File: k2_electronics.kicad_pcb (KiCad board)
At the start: 2 copper layers, 152.1 x 87.5 mm, 58 parts, among them SW1 SW_SPST, SW10 SW_SPST, SW11 SW_SPST, SW12 SW_SPST, SW13 SW_SPST, SW14 SW_SPST, SW15 SW_SPST, SW16 SW_SPST, SW17 SW_SPST, SW18 SW_SPST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

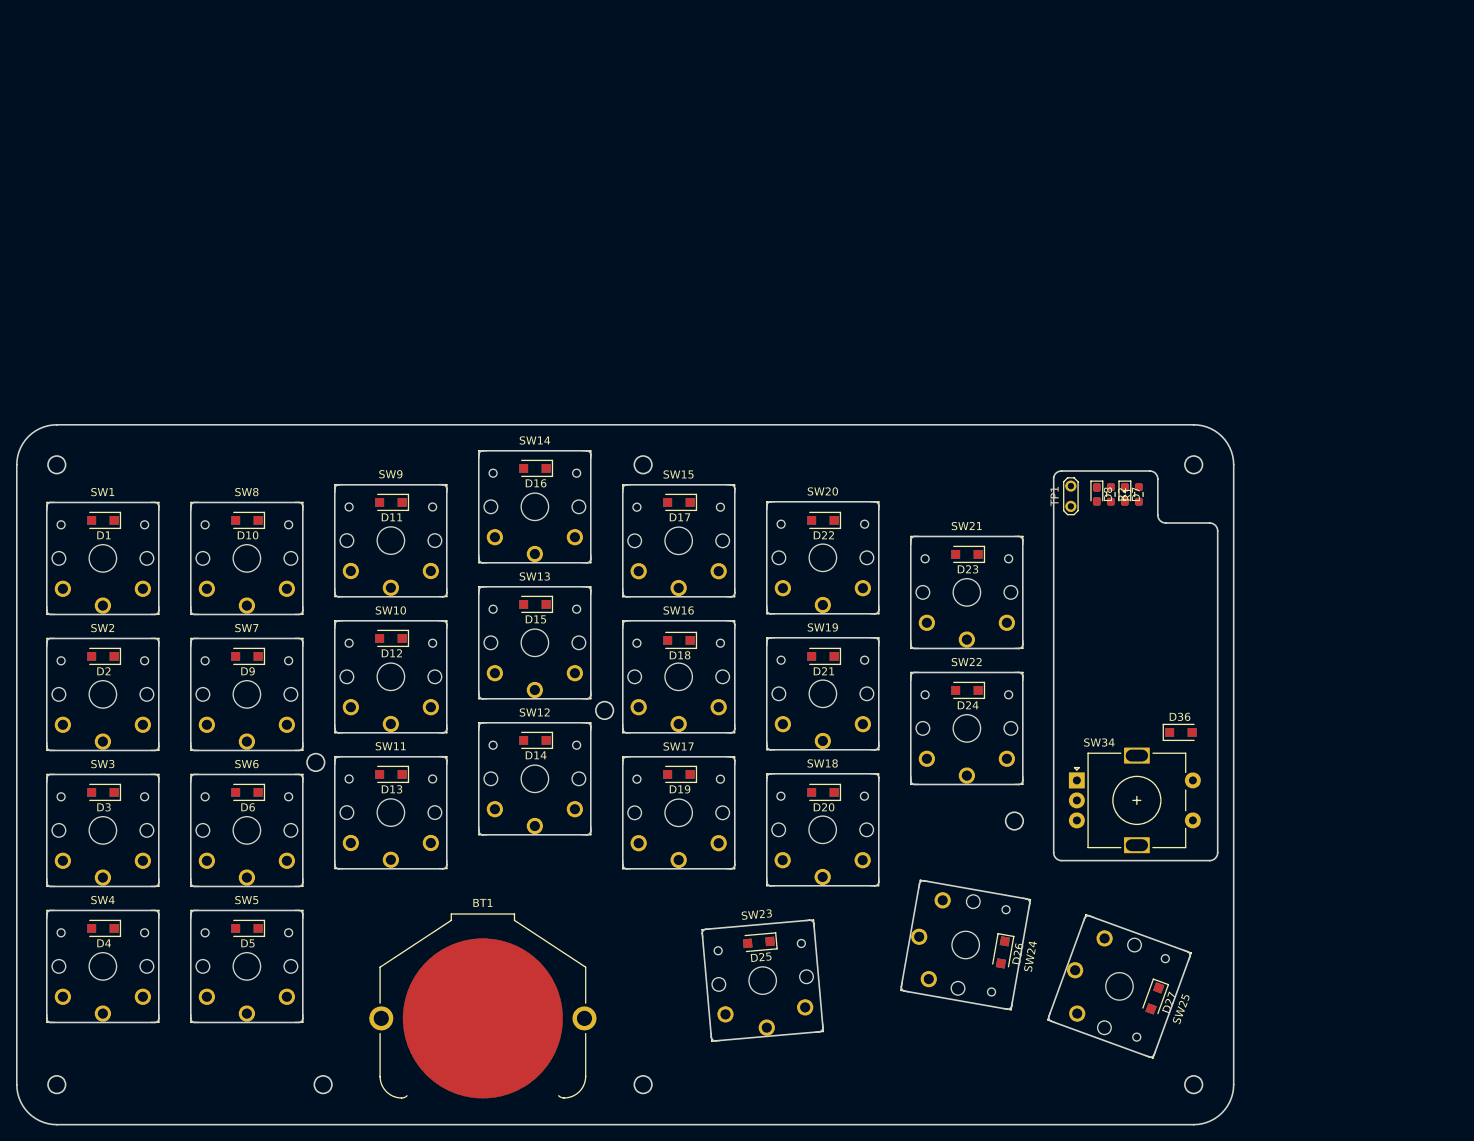
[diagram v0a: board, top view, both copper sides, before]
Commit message: Component placement and autoroute
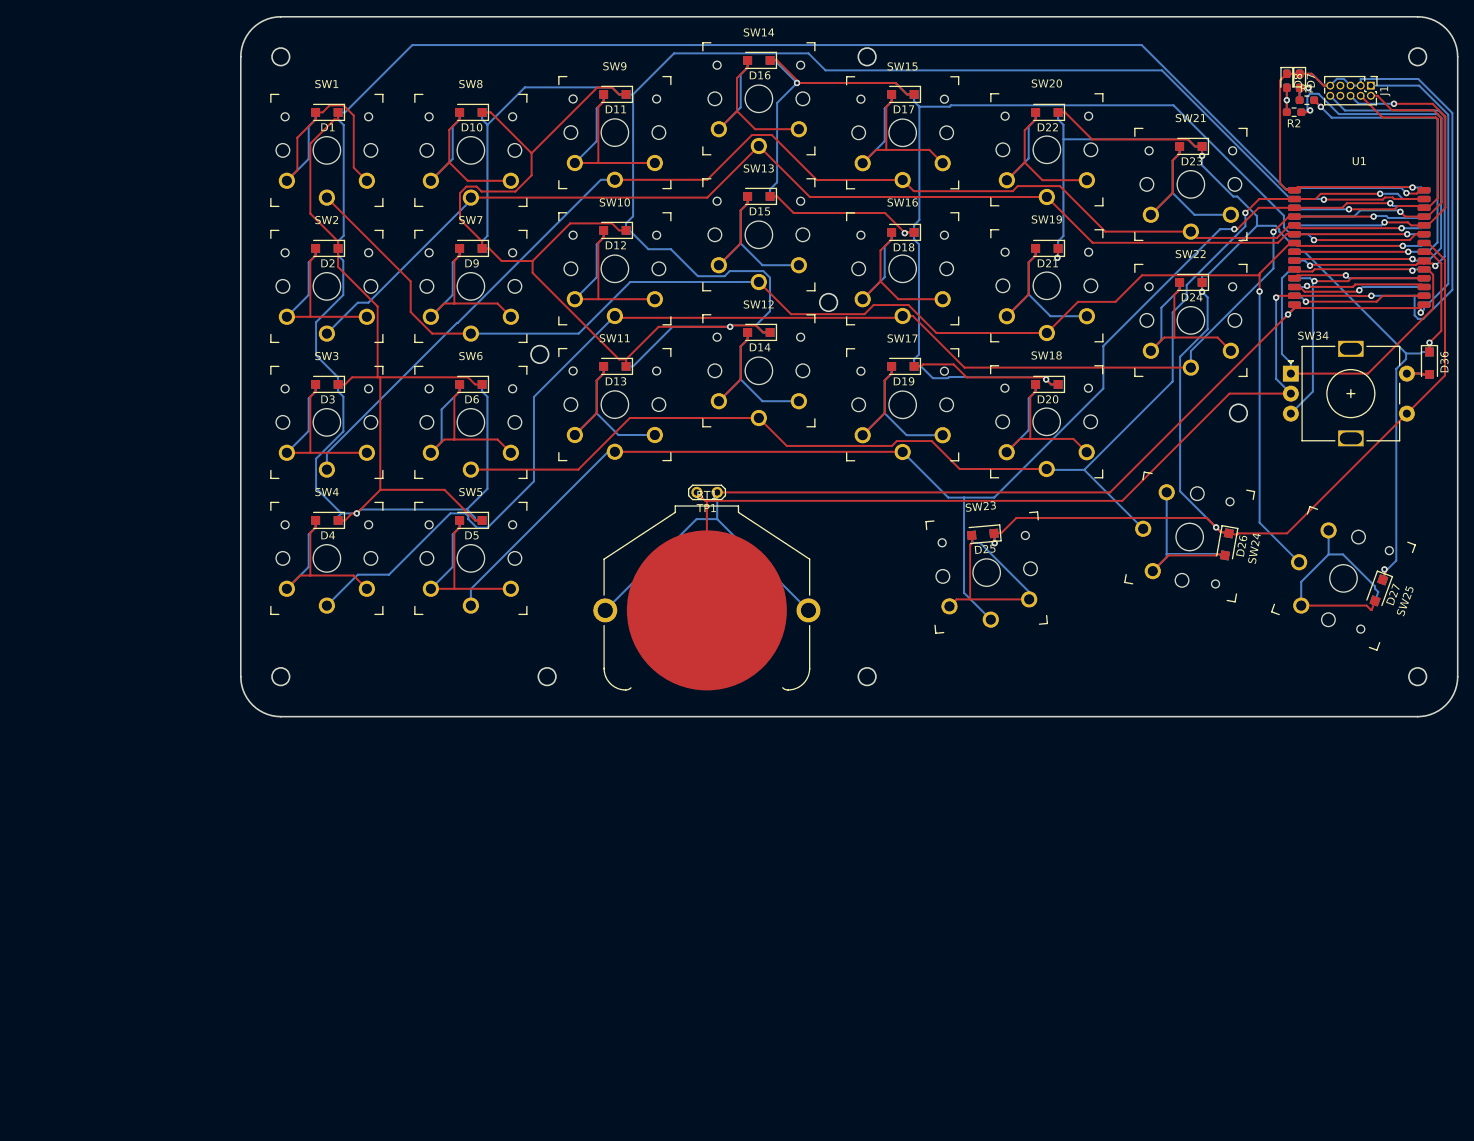
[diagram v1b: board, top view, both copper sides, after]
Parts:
- added J1: Conn_ARM_JTAG_SWD_10, Connector_PinHeader_1.27mm:PinHeader_2x05_P1.27mm_Vertical, F.Cu at (221.5, 58.9)
- added U1: MS88SF2, k2:MS88F2_reversible, F.Cu at (220.1, 75.9)
- moved BT1 58.2 mm to (138.5, 124.5)
- moved D1 58.2 mm to (91.0, 62.2)
- moved D10 58.2 mm to (109.0, 62.2)
- moved D11 58.2 mm to (127.0, 60.0)
- moved D12 58.2 mm to (127.0, 77.0)
- moved D13 58.2 mm to (127.0, 94.0)
- moved D14 58.2 mm to (145.0, 89.8)
- moved D15 58.2 mm to (145.0, 72.8)
- moved D16 58.2 mm to (145.0, 55.8)
- moved D17 58.2 mm to (163.0, 60.0)
- moved D18 58.2 mm to (163.0, 77.2)
- moved D19 58.2 mm to (163.0, 94.0)
- moved D2 58.2 mm to (91.0, 79.2)
- moved D20 58.2 mm to (181.0, 96.2)
- moved D21 58.2 mm to (181.0, 79.2)
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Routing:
- net Net-(D1-Pad1): track 0.00 -> 332.7 mm, vias 0 -> 2
- net Net-(D10-Pad1): track 0.00 -> 317.2 mm, vias 0 -> 2
- net Net-(D15-Pad1): track 0.00 -> 221.2 mm, vias 0 -> 4
- net GND: track 0.00 -> 219.8 mm, vias 0 -> 3
- net Net-(D21-Pad1): track 0.00 -> 211.5 mm, vias 0 -> 5
- net Net-(SW1-Pad1): track 0.00 -> 195.7 mm, vias 0 -> 2
- net VDD: track 0.00 -> 176.5 mm, vias 0 -> 2
- net Net-(SW10-Pad1): track 0.00 -> 174.8 mm, vias 0 -> 2
- net Net-(SW11-Pad1): track 0.00 -> 165.9 mm, vias 0 -> 2
- net Net-(SW15-Pad1): track 0.00 -> 162.5 mm, vias 0 -> 1
- net Net-(SW12-Pad1): track 0.00 -> 157.0 mm, vias 0 -> 2
- net Net-(SW14-Pad1): track 0.00 -> 152.5 mm, vias 0 -> 1
- net Net-(D27-Pad1): track 0.00 -> 68.9 mm, vias 0 -> 2
- net Net-(R2-Pad1): track 0.00 -> 57.6 mm, vias 0 -> 2
- net /~RESET: track 0.00 -> 53.1 mm, vias 0 -> 2
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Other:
- outline, holes or cut-outs redrawn

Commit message: Ensure all footprints reversible and touchup
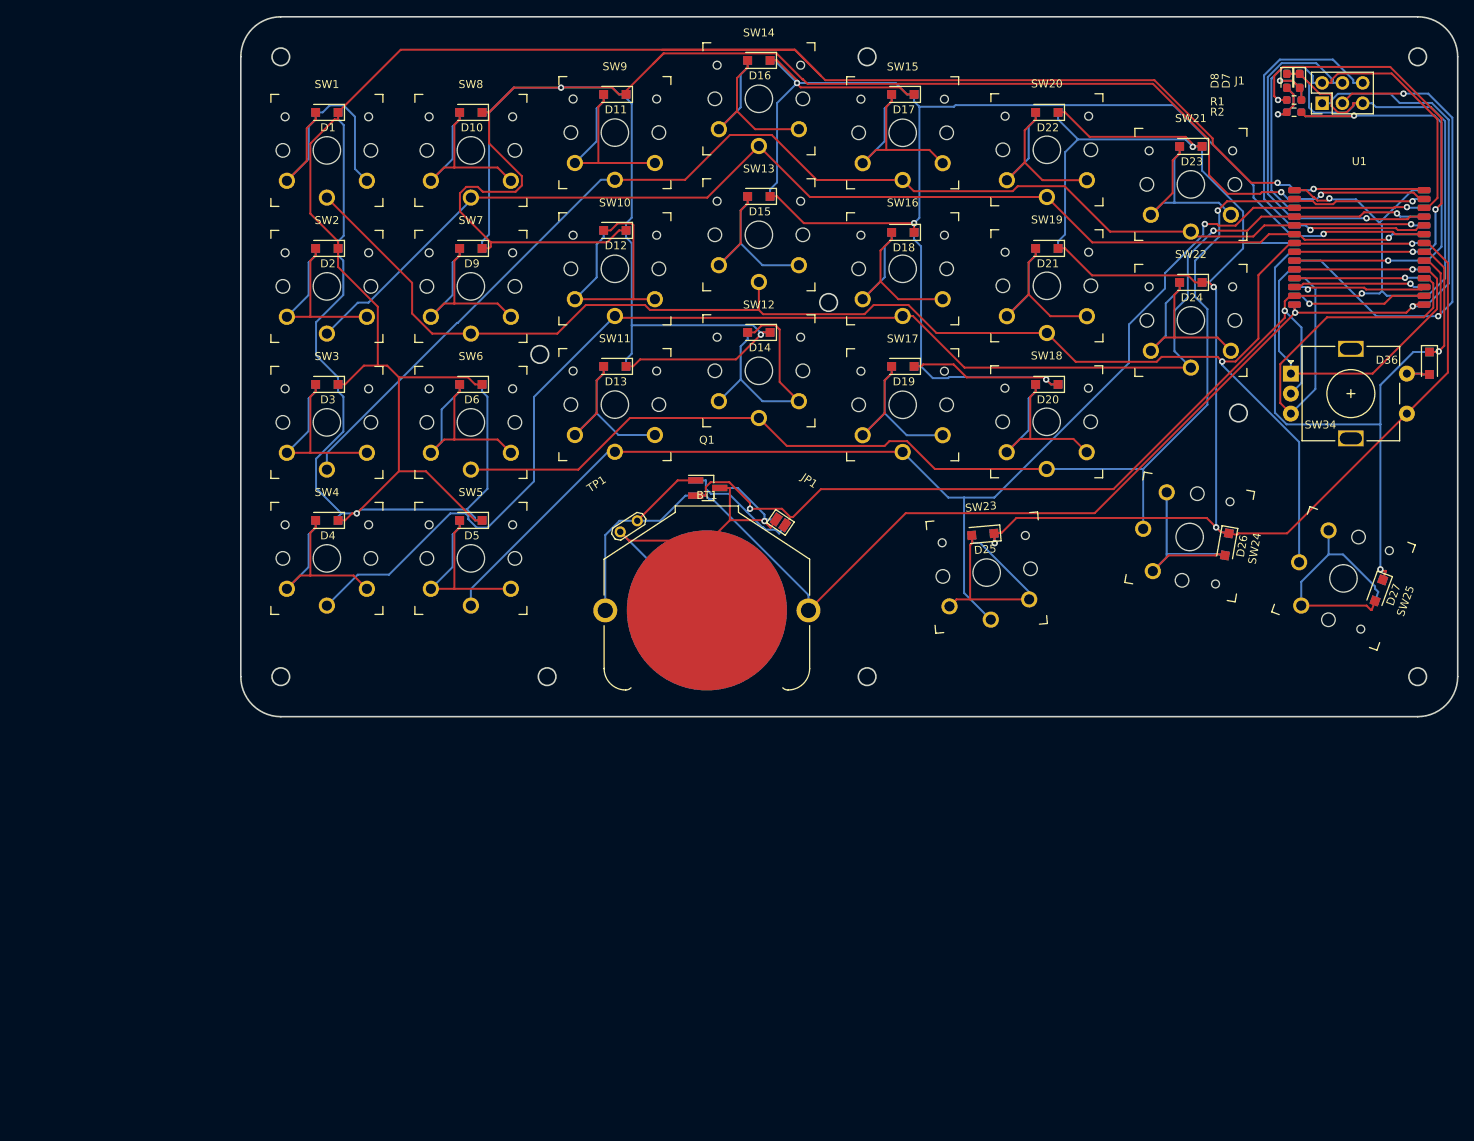
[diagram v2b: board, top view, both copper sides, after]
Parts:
- added JP1: SolderJumper_2_Open, k2:SolderJumper-2_P1.3mm_Open_Pad1.0x1.5mm_reversible, F.Cu at (147.7, 113.5)
- added Q1: Q_NMOS_GSD, k2:SOT-23_Handsoldering_reversible, F.Cu at (138.6, 109.2)
- BT1: footprint Battery:BatteryHolder_Keystone_3009_1x2450 -> k2:BatteryHolder_Keystone_3009_1x2450_reversible
- J1: value Conn_ARM_JTAG_SWD_10 -> Conn_02x03_Odd_Even; footprint Connector_PinHeader_1.27mm:PinHeader_2x05_P1.27mm_Vertical -> Connector_PinHeader_2.54mm:PinHeader_2x03_P2.54mm_Vertical
- moved TP1 10.6 mm to (129.8, 113.3), turned to 213 degrees
- moved J1 6.48 mm to (215.4, 61.1), turned to 90 degrees
- moved R1 1.60 mm to (211.9, 60.7), turned to 180 degrees
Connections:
- BT1 pad 2: GND -> Net-(BT1-Pad2)
- J1 pad 2: /SWDIO -> /SWCLK
- J1 pad 3: GND -> /~RESET
- J1 pad 4: /SWCLK -> /SWDIO
- TP1 pad 2: GND -> Net-(BT1-Pad2)
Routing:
- net Net-(BT1-Pad2): track 0.00 -> 60.2 mm, vias 0 -> 1
- net Net-(D10-Pad1): track 317.2 -> 291.3 mm, vias 2 -> 4
- net Net-(D1-Pad1): track 332.7 -> 352.7 mm, vias 2 -> 3
- net Net-(SW34-PadB): track 34.2 -> 53.3 mm, vias 1 -> 0
- net Net-(D27-Pad1): track 68.9 -> 86.5 mm
- net /~RESET: track 53.1 -> 70.1 mm
- net /SWCLK: track 39.5 -> 55.6 mm, vias 1 -> 0
- net VDD: track 176.5 -> 192.2 mm
- net Net-(D21-Pad1): track 211.5 -> 224.3 mm, vias 5 -> 4
- net Net-(R1-Pad2): track 51.4 -> 63.5 mm, vias 2 -> 3
- net /SWO: track 44.4 -> 52.1 mm, vias 2 -> 1
- net /SWDIO: track 40.3 -> 46.9 mm
- net Net-(SW10-Pad1): track 174.8 -> 181.2 mm
- net GND: track 219.8 -> 226.2 mm, vias 3 -> 4
- net Net-(SW12-Pad1): track 157.0 -> 161.8 mm
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
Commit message: Prepare for the worst
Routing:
- net VDD: track 192.2 -> 193.7 mm
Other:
- board text added: "Dan Stutman 2021"
- board text added: "K2.0"

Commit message: Store for deletions
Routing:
- net Net-(D27-Pad2): track 30.6 -> 29.8 mm
- net Net-(D27-Pad1): track 86.5 -> 86.0 mm
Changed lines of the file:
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@@
     (thickness 1.6)
     (drawings 94)
-    (tracks 1073)
+    (tracks 1068)
     (zones 0)
     (modules 62)
@@
   (segment (start 168.8252 123.9963) (end 169.6967 123.1248) (width 0.25) (layer F.Cu) (net 29) (status 10))
   (segment (start 169.6967 123.1248) (end 171.4078 123.1248) (width 0.25) (layer F.Cu) (net 29))
-  (segment (start 171.4078 123.1248) (end 171.4078 116.3508) (width 0.25) (layer F.Cu) (net 29))
-  (segment (start 171.4078 116.3508) (end 171.6883 116.0703) (width 0.25) (layer F.Cu) (net 29))
-  (segment (start 171.6053 115.122) (end 171.6883 116.0703) (width 0.25) (layer F.Cu) (net 29) (status 10))
   (segment (start 171.6053 115.122) (end 171.6883 116.0703) (width 0.25) (layer B.Cu) (net 29) (status 10))
   (segment (start 178.7872 123.1248) (end 178.7872 122.1994) (width 0.25) (layer B.Cu) (net 29) (status 30))
   (segment (start 178.7872 122.1994) (end 172.6581 116.0703) (width 0.25) (layer B.Cu) (net 29) (status 10))
   (segment (start 172.6581 116.0703) (end 171.6883 116.0703) (width 0.25) (layer B.Cu) (net 29))
-  (segment (start 203.2569 117.6287) (end 202.2428 117.4499) (width 0.25) (layer F.Cu) (net 30) (status 10))
-  (segment (start 202.2428 117.4499) (end 202.2428 117.45) (width 0.25) (layer F.Cu) (net 30))
-  (segment (start 202.2428 117.45) (end 202.0641 117.6287) (width 0.25) (layer F.Cu) (net 30))
-  (segment (start 202.0641 117.6287) (end 196.2 117.6287) (width 0.25) (layer F.Cu) (net 30))
-  (segment (start 196.2 117.6287) (end 194.2395 119.5892) (width 0.25) (layer F.Cu) (net 30) (status 20))
+  (segment (start 171.4078 115.319545) (end 171.605327 115.122018) (width 0.25) (layer F.Cu) (net 29))
+  (segment (start 171.4078 123.1248) (end 171.4078 115.319545) (width 0.25) (layer F.Cu) (net 29))
   (segment (start 195.976 117.45) (end 195.976 117.8527) (width 0.25) (layer B.Cu) (net 30))
   (segment (start 195.976 117.8527) (end 194.2395 119.5892) (width 0.25) (layer B.Cu) (net 30) (status 20))
@@
   (segment (start 202.2428 117.45) (end 202.2428 117.4499) (width 0.25) (layer B.Cu) (net 30))
   (segment (start 203.2569 117.6287) (end 202.2428 117.4499) (width 0.25) (layer B.Cu) (net 30) (status 10))
+  (segment (start 203.256862 117.6287) (end 203.256893 117.628731) (width 0.25) (layer F.Cu) (net 30))
+  (segment (start 196.2 117.6287) (end 203.256862 117.6287) (width 0.25) (layer F.Cu) (net 30))
+  (segment (start 194.2395 119.5892) (end 196.2 117.6287) (width 0.25) (layer F.Cu) (net 30))
   (segment (start 222.0212 123.3156) (end 222.4295 122.1936) (width 0.25) (layer B.Cu) (net 31) (status 10))
   (segment (start 216.2143 117.5082) (end 218.0188 117.5082) (width 0.25) (layer B.Cu) (net 31))
@@
   (segment (start 216.2143 117.5082) (end 212.7941 120.9284) (width 0.25) (layer B.Cu) (net 31))
   (segment (start 212.7941 120.9284) (end 212.7941 123.8988) (width 0.25) (layer B.Cu) (net 31) (status 20))
-  (segment (start 222.0212 123.3156) (end 221.6129 124.4375) (width 0.25) (layer F.Cu) (net 31) (status 10))
-  (segment (start 212.7941 123.8988) (end 220.9592 123.8988) (width 0.25) (layer F.Cu) (net 31) (status 10))
-  (segment (start 220.9592 123.8988) (end 221.4979 124.4375) (width 0.25) (layer F.Cu) (net 31))
-  (segment (start 221.4979 124.4375) (end 221.6129 124.4375) (width 0.25) (layer F.Cu) (net 31))
+  (segment (start 221.437942 123.8988) (end 222.021172 123.31557) (width 0.25) (layer F.Cu) (net 31))
+  (segment (start 212.7941 123.8988) (end 221.437942 123.8988) (width 0.25) (layer F.Cu) (net 31))
   (segment (start 229.9784 92.1238) (end 230.6733 91.4289) (width 0.25) (layer F.Cu) (net 32))
   (segment (start 230.6733 91.4289) (end 230.6733 81.6646) (width 0.25) (layer F.Cu) (net 32))
@@
   (segment (start 209.5069 81.6545) (end 211.4864 79.675) (width 0.25) (layer B.Cu) (net 32) (status 20))
   (segment (start 211.4864 79.675) (end 211.95 79.675) (width 0.25) (layer B.Cu) (net 32) (status 30))
-  (segment (start 223.3871 119.5625) (end 222.8846 119.5625) (width 0.25) (layer B.Cu) (net 32))
   (segment (start 222.8846 119.5625) (end 222.7877 119.4656) (width 0.25) (layer B.Cu) (net 32))
   (segment (start 222.7877 119.4656) (end 222.7876 119.4656) (width 0.25) (layer B.Cu) (net 32))
   (segment (start 222.7876 119.4656) (end 222.6908 119.3688) (width 0.25) (layer B.Cu) (net 32))
-  (segment (start 222.9788 120.6844) (end 223.3871 119.5625) (width 0.25) (layer B.Cu) (net 32) (status 10))
-  (segment (start 222.9788 120.6844) (end 223.3871 119.5625) (width 0.25) (layer F.Cu) (net 32) (status 10))
-  (segment (start 223.3871 119.5625) (end 222.8845 119.5625) (width 0.25) (layer F.Cu) (net 32))
   (segment (start 222.8845 119.5625) (end 222.6908 119.3688) (width 0.25) (layer F.Cu) (net 32))
   (segment (start 228.825 92.2) (end 229.7003 92.2) (width 0.25) (layer F.Cu) (net 32) (status 10))
   (via (at 222.6908 119.3688) (size 0.8) (layers F.Cu B.Cu) (net 32))
   (via (at 229.9784 92.1238) (size 0.8) (layers F.Cu B.Cu) (net 32))
+  (segment (start 222.978828 119.656828) (end 222.6908 119.3688) (width 0.25) (layer F.Cu) (net 32))
+  (segment (start 222.978828 120.68443) (end 222.978828 119.656828) (width 0.25) (layer F.Cu) (net 32))
+  (segment (start 222.6908 120.396402) (end 222.978828 120.68443) (width 0.25) (layer B.Cu) (net 32))
+  (segment (start 222.6908 119.3688) (end 222.6908 120.396402) (width 0.25) (layer B.Cu) (net 32))
   (segment (start 228.825 95) (end 227.9497 95) (width 0.25) (layer F.Cu) (net 33) (status 10))
   (segment (start 226 94.9) (end 227.8497 94.9) (width 0.25) (layer F.Cu) (net 33) (status 10))

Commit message: Reroute
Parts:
- moved J1 5.59 mm to (220.4, 58.6), turned to 270 degrees
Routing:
- net Net-(D15-Pad1): track 220.4 -> 294.7 mm, vias 4 -> 3
- net Net-(D21-Pad1): track 224.3 -> 257.9 mm, vias 4 -> 5
- net GND: track 226.2 -> 194.1 mm, vias 4 -> 3
- net Net-(SW12-Pad1): track 161.8 -> 192.7 mm, vias 2 -> 1
- net Net-(BT1-Pad2): track 60.2 -> 88.4 mm, vias 1 -> 0
- net Net-(R1-Pad2): track 63.5 -> 40.8 mm
- net Net-(D1-Pad1): track 352.7 -> 372.5 mm, vias 3 -> 2
- net /SWO: track 52.1 -> 71.3 mm
- net VDD: track 193.7 -> 210.5 mm
- net Net-(SW1-Pad1): track 195.7 -> 212.0 mm
- net /SWCLK: track 55.6 -> 40.3 mm, vias 0 -> 1
- net Net-(D27-Pad1): track 86.0 -> 71.4 mm
- net /~RESET: track 70.1 -> 55.7 mm, vias 2 -> 1
- net Net-(D10-Pad1): track 291.3 -> 305.3 mm, vias 4 -> 3
- net Net-(SW34-PadB): track 53.3 -> 45.5 mm, vias 0 -> 1
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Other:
- net class Default: trace_width 0.25 -> 0.3
- board text added: "JLCJLCJLCJLC"
